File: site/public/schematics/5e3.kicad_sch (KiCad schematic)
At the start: 44 parts, among them T2 8k:8

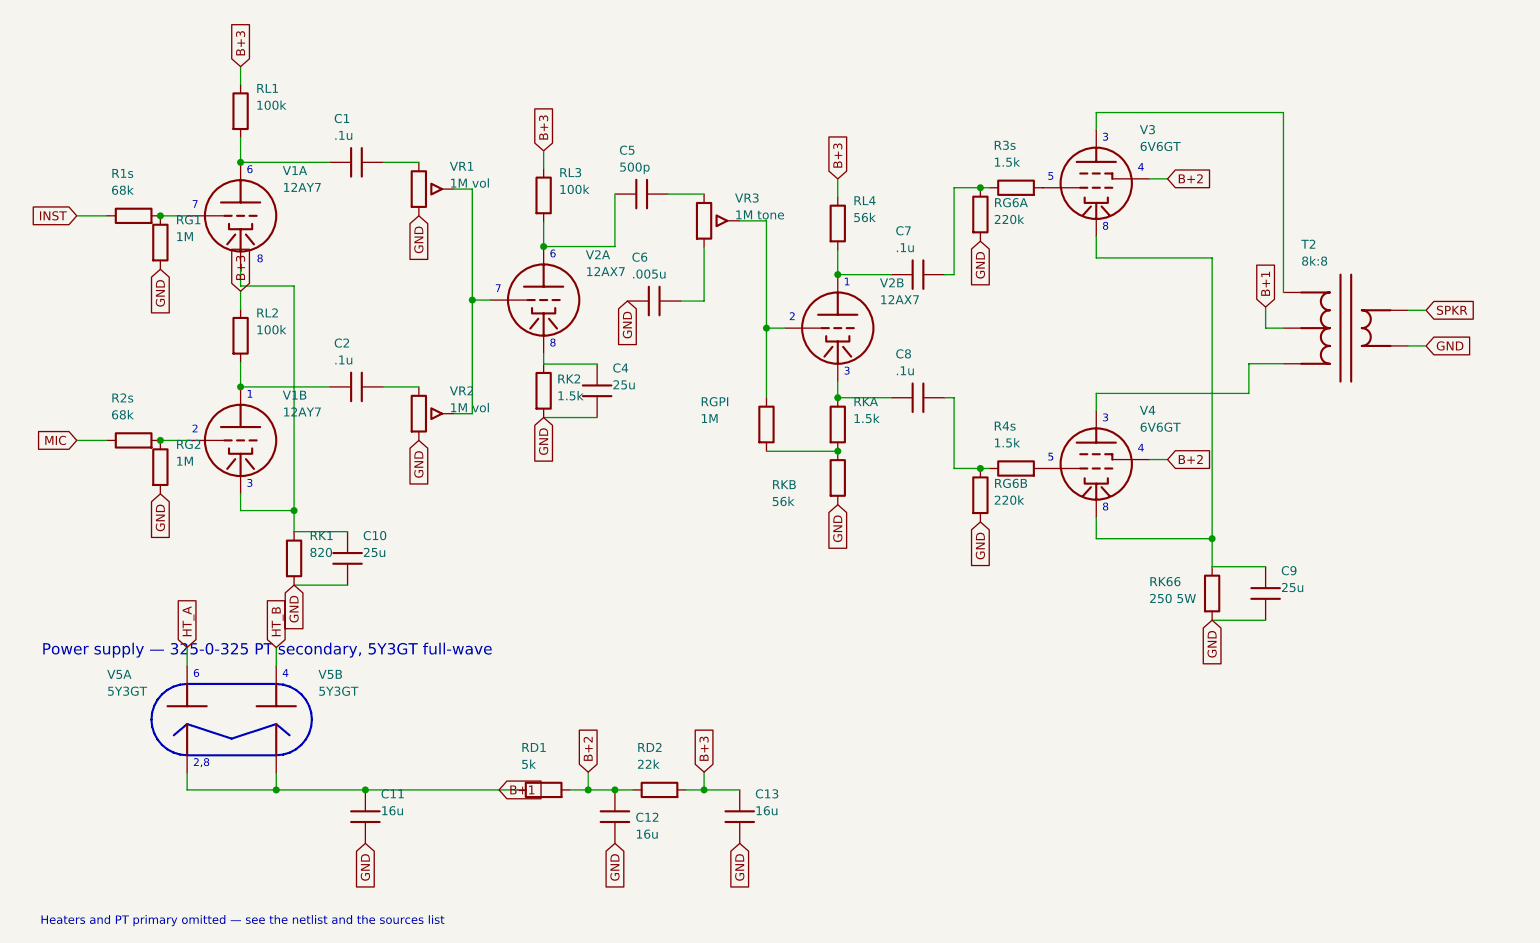
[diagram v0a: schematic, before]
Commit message: Re-export the worklists, public copies and card for the 5E3 audit fixes
- sheet-board.yaml: 5E3 now has unresolved 0 (VR3#ends cleared), and C5,
  C6, RG1 and RG2 are no longer sheet-only. Two-terminal parts checked go
  from 28 to 36.
- verification-freshness.yaml: 5E3 (never stamped) gets its new current
  facts fingerprint. It stays verified and on the worklist. Nothing is
  stamped.
- site/public schematic and layout copies and the 5E3 social card are
  regenerated.

Co-Authored-By: Claude Opus 5.5 <noreply@anthropic.com>
Claude-Session: https://claude.ai/code/session_01KBMfdh37HmCL2iWcBiL5J1
Signed-off-by: AnalogMaker <theanalogmaker@gmail.com>
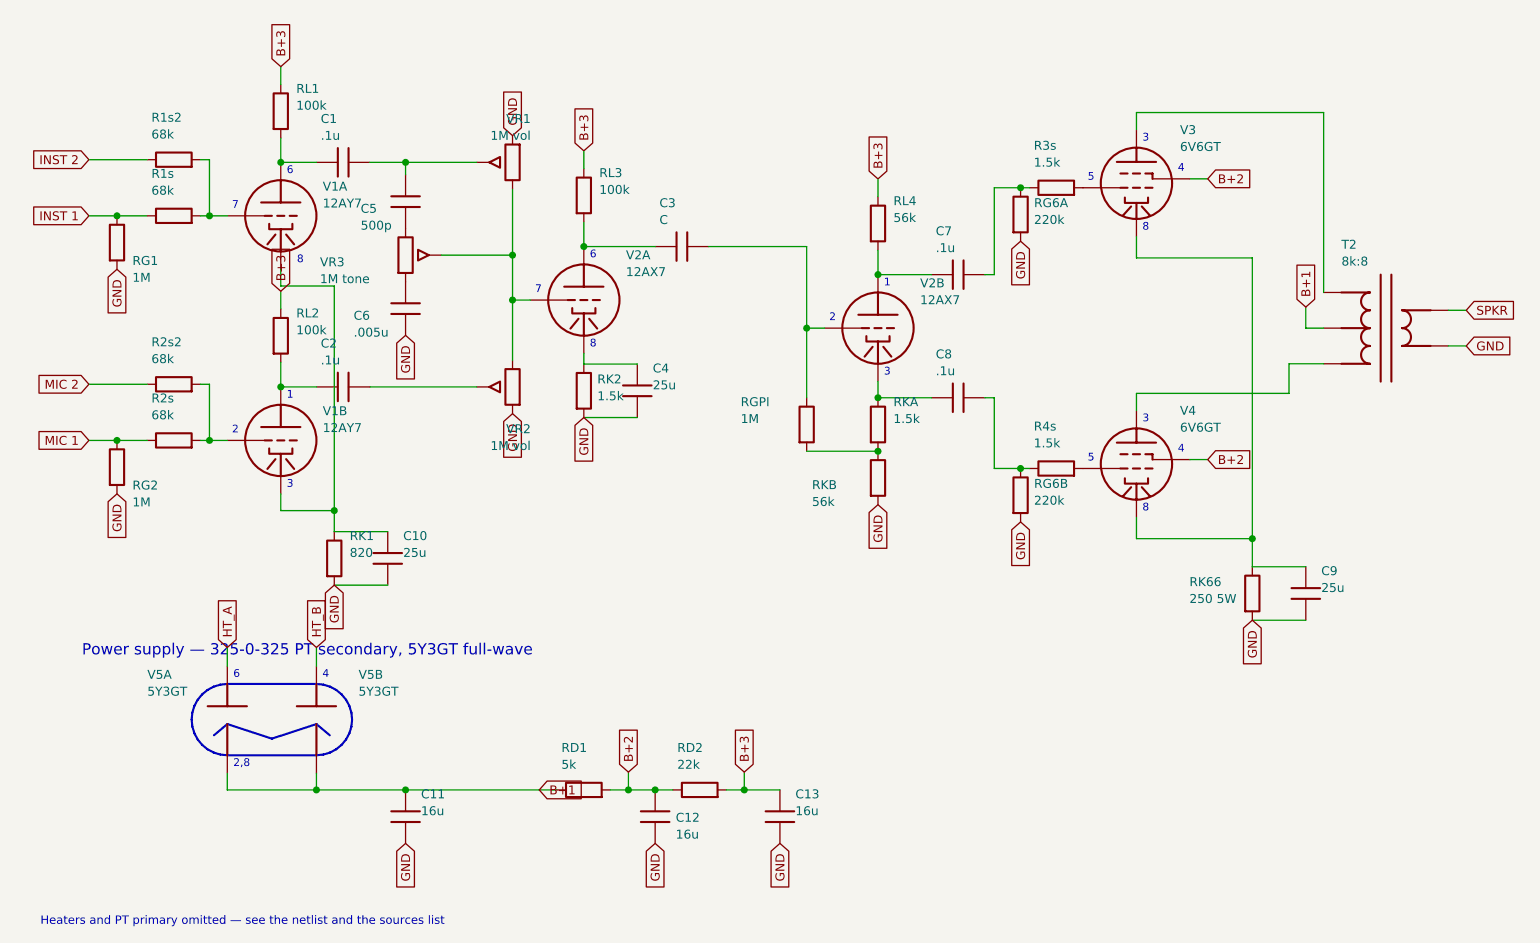
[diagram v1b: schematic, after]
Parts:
- removed C10: 25u, symbol cx:C
- removed R2s: 68k, symbol cx:R
- removed RGPI: 1M, symbol cx:R
- removed RL1, RL3: 100k, symbol cx:R
- removed V4: 6V6GT, symbol cx:PENTODE
- removed V5A: 5Y3GT, symbol cx:DIODE_TUBE
- removed VR1: 1M vol, symbol cx:POT
- added C2, C7, C8: .1u, symbol cx:C
- added C3: C, symbol cx:C
- added C9: 25u, symbol cx:C
- added R1s2, R2s2: 68k, symbol cx:R
- added RD1: 5k, symbol cx:R
- added RL2: 100k, symbol cx:R
- added V1B: 12AY7, symbol cx:TRIODE
- added V3: 6V6GT, symbol cx:PENTODE
- C10: renamed from C2; value .1u -> 25u
- R2s: renamed from RL2; value 100k -> 68k
- RGPI: renamed from V3; value 6V6GT -> 1M; symbol cx:PENTODE -> cx:R
- RK2: renamed from V2B; value 12AX7 -> 1.5k; symbol cx:TRIODE -> cx:R
- RKA: renamed from C8; value .1u -> 1.5k; symbol cx:C -> cx:R
- RL1: renamed from V1B; value 12AY7 -> 100k; symbol cx:TRIODE -> cx:R
- RL3: renamed from RKA; value 1.5k -> 100k
- V2B: renamed from C7; value .1u -> 12AX7; symbol cx:C -> cx:TRIODE
- V4: renamed from C9; value 25u -> 6V6GT; symbol cx:C -> cx:PENTODE
- V5A: renamed from RD1; value 5k -> 5Y3GT; symbol cx:R -> cx:DIODE_TUBE
- VR1: renamed from RK2; value 1.5k -> 1M vol; symbol cx:R -> cx:POT
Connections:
- net B+1: now also V5A.2 (K), RD1.1; no longer V5A.1
- net B+2: now also RD2.1, V4.3 (G2), RD1.2, V3.3 (G2); no longer RGPI.3 (G2), V5A.2
- net B+3: now also RL1.1, RL3.1, RL2.1; no longer R2s.1
- net GND: now also C10.2, C6.2, RK2.2, VR1.3, C9.2; no longer V4.2, VR1.2
- net HT_A: now also V5A.1 (A)
- net at R4s.1, RG6B.1: now also C8.2; no longer RKA.2
- net at R4s.2: now also V4.2 (G1)
- net at C6.1: now also VR3.3
- net at C5.1: now also C1.2, VR1.2 (W); no longer V2A.1 (P)
- net at C5.2: now also VR3.1
- net at V2A.2 (G): now also VR1.1, VR2.1, VR3.2 (W); no longer VR2.2 (W)
- net at R3s.1, RG6A.1: now also C7.2; no longer V2B.2
- net at RL4.2, V2B.1 (P): now also C7.1; no longer RK2.1 (P)
- net at C1.1, V1A.1 (P): now also RL1.2
- net MIC 1: now reaches RG2.1
- net MIC 1: now also R2s.1; no longer RL1.2 (G)
- net at RK1.1, V1A.3 (K): now also C10.1, V1B.3 (K); no longer RL1.3 (K)
- net at R1s.2, V1A.2 (G): now also R1s2.2; no longer RG1.1
- net at RGPI.2: now also RKA.2, RKB.1; no longer R3s.2
- net at C4.1, V2A.3 (K): now also RK2.1; no longer VR1.1
- net at RGPI.1: now also V2B.2 (G), C3.2; no longer T2.1 (PRI_A)
- net at T2.3 (PRI_B): now also V4.1 (P)
- net at RL3.2: now also V2A.1 (P), C3.1; no longer RKB.1
- net INST renamed INST 1
- net INST 1: now also RG1.1
- new net: R2s.2, R2s2.2, V1B.2 (G)
- new net: C8.1, RKA.1, V2B.3 (K)
- new net: C9.1, RK66.1, V3.4 (K), V4.4 (K)
- new net: C2.1, RL2.2, V1B.1 (P)
- new net: C2.2, VR2.2 (W)
- new net: T2.1 (PRI_A), V3.1 (P)
- new net: R3s.2, V3.2 (G1)
- new net INST 2: R1s2.1
- new net MIC 2: R2s2.1
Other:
- moved on the sheet: C10, R2s, RL3, V1A, VR3
